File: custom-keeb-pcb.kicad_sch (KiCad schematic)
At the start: 34 parts, among them SW1 SW_Push, SW2 RotaryEncoder_Switch, U1 ATmega32U4-A, Y1 16MHz

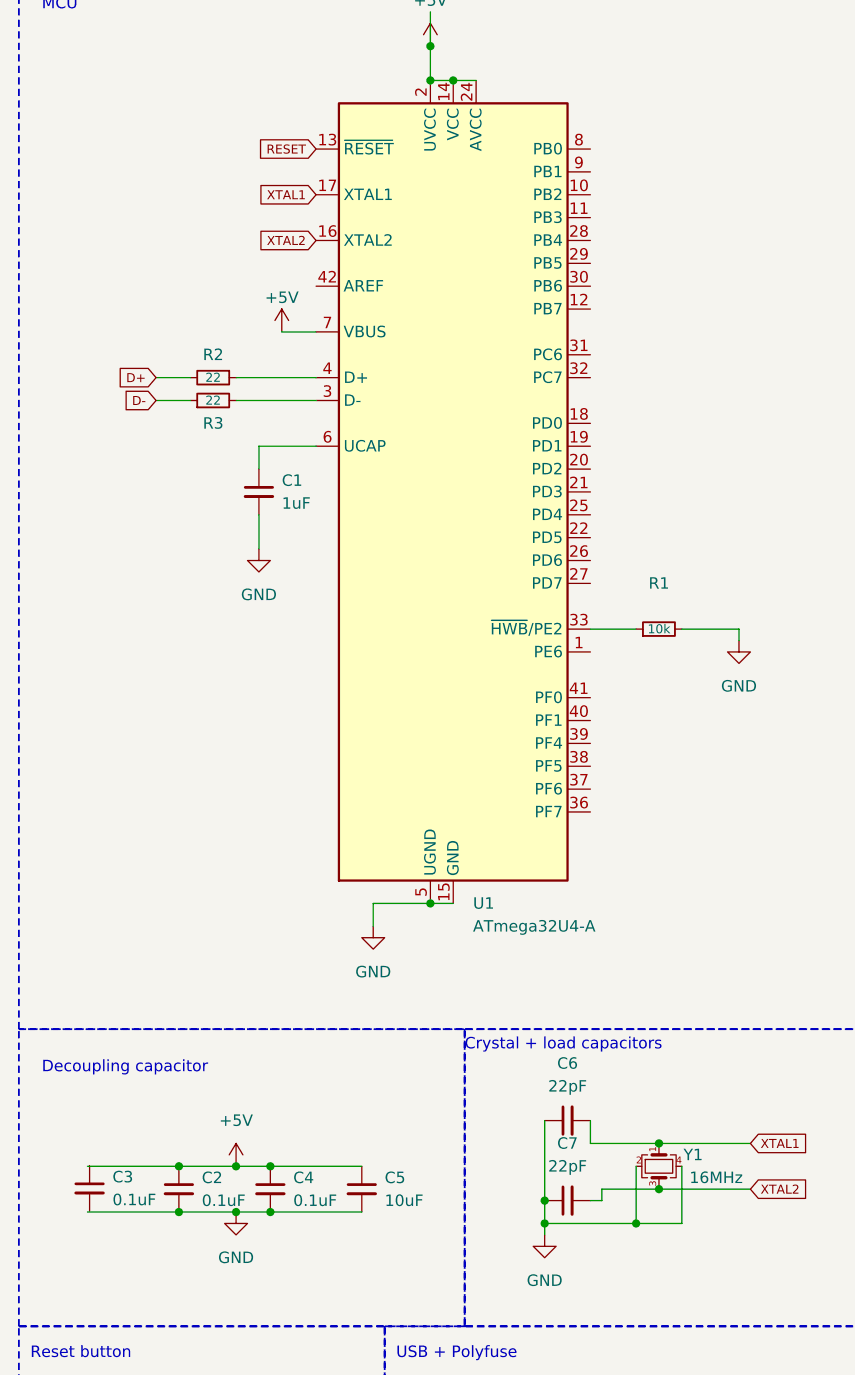
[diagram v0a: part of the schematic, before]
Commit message: Completed v1 of PCB design
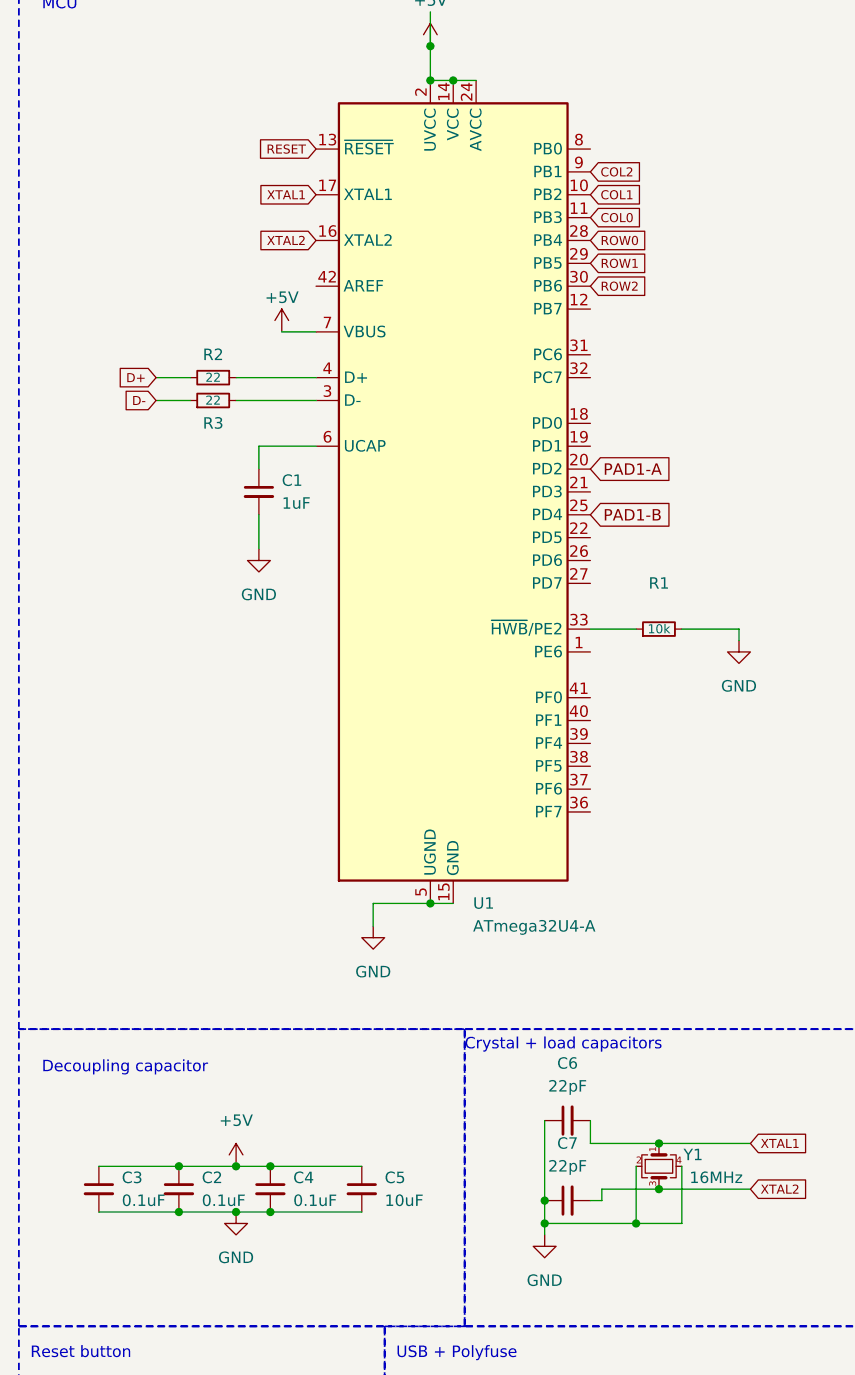
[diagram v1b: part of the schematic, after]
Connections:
- net +5V: now also C3.1
- net COL0: now also U1.11 (PB3)
- net COL1: now also U1.10 (PB2)
- net COL2: now also U1.9 (PB1)
- net GND: now also C3.2
- net PAD1-A: now also U1.20 (PD2)
- net PAD1-B: now also U1.25 (PD4)
- net ROW0: now also U1.28 (PB4)
- net ROW1: now also U1.29 (PB5)
- net ROW2: now also U1.30 (PB6)
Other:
- moved on the sheet: C3
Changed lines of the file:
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@@
   (junction (at 81.28 151.13) (diameter 0) (color 0 0 0 0)
   )
+  (junction (at 161.29 50.8) (diameter 0) (color 0 0 0 0)
+  )
+  (junction (at 30.48 149.86) (diameter 0) (color 0 0 0 0)
+  )
+  (junction (at 71.12 151.13) (diameter 0) (color 0 0 0 0)
+  )
+  (junction (at 153.67 76.2) (diameter 0) (color 0 0 0 0)
+  )
   (junction (at 30.48 144.78) (diameter 0) (color 0 0 0 0)
   )
-  (junction (at 161.29 50.8) (diameter 0) (color 0 0 0 0)
-  )
-  (junction (at 71.12 151.13) (diameter 0) (color 0 0 0 0)
-  )
-  (junction (at 153.67 76.2) (diameter 0) (color 0 0 0 0)
-  )
   (junction (at 186.69 66.04) (diameter 0) (color 0 0 0 0)
   )
@@
   (junction (at 173.99 66.04) (diameter 0) (color 0 0 0 0)
   )
-  (junction (at 30.48 149.86) (diameter 0) (color 0 0 0 0)
-  )
   (junction (at 83.82 147.32) (diameter 0) (color 0 0 0 0)
   )
@@
     (stroke (width 0) (type default))
   )
-  (wire (pts (xy 20.32 149.86) (xy 30.48 149.86))
-    (stroke (width 0) (type default))
-  )
   (wire (pts (xy 161.29 43.18) (xy 161.29 50.8))
     (stroke (width 0) (type default))
@@
     (stroke (width 0) (type default))
   )
-  (wire (pts (xy 20.32 144.78) (xy 30.48 144.78))
-    (stroke (width 0) (type default))
-  )
   (wire (pts (xy 166.37 71.12) (xy 168.91 71.12))
     (stroke (width 0) (type default))
@@
     (stroke (width 0) (type default))
   )
+  (wire (pts (xy 21.59 144.78) (xy 30.48 144.78))
+    (stroke (width 0) (type default))
+  )
   (wire (pts (xy 80.01 180.34) (xy 87.63 180.34))
     (stroke (width 0) (type default))
@@
   )
   (wire (pts (xy 77.47 147.32) (xy 83.82 147.32))
+    (stroke (width 0) (type default))
+  )
+  (wire (pts (xy 21.59 149.86) (xy 30.48 149.86))
     (stroke (width 0) (type default))
   )
@@
   (text "Decoupling capacitor" (at 15.24 134.62 0)
     (effects (font (size 1.27 1.27)) (justify left bottom))
+  )
+  (global_label "ROW1" (shape input) (at 76.2 44.45 0) (fields_autoplaced)
+    (effects (font (size 1 1)) (justify left))
+    (property "Intersheetrefs" "${INTERSHEET_REFS}" (at 82.6932 44.45 0)
+      (effects (font (size 1.27 1.27)) (justify left) hide)
+    )
+  )
+  (global_label "ROW0" (shape input) (at 76.2 41.91 0) (fields_autoplaced)
+    (effects (font (size 1 1)) (justify left))
+    (property "Intersheetrefs" "${INTERSHEET_REFS}" (at 82.6932 41.91 0)
+      (effects (font (size 1.27 1.27)) (justify left) hide)
+    )
+  )
+  (global_label "PAD1-B" (shape input) (at 76.2 72.39 0) (fields_autoplaced)
+    (effects (font (size 1.27 1.27)) (justify left))
+    (property "Intersheetrefs" "${INTERSHEET_REFS}" (at 86.8657 72.39 0)
+      (effects (font (size 1.27 1.27)) (justify left) hide)
+    )
   )
   (global_label "XTAL2" (shape input) (at 93.98 147.32 0) (fields_autoplaced)
@@
     )
   )
+  (global_label "ROW2" (shape input) (at 76.2 46.99 0) (fields_autoplaced)
+    (effects (font (size 1 1)) (justify left))
+    (property "Intersheetrefs" "${INTERSHEET_REFS}" (at 82.6932 46.99 0)
+      (effects (font (size 1.27 1.27)) (justify left) hide)
+    )
+  )
   (global_label "ROW1" (shape input) (at 142.24 76.2 180) (fields_autoplaced)
     (effects (font (size 1 1)) (justify right))
@@
     )
   )
+  (global_label "COL1" (shape input) (at 76.2 36.83 0) (fields_autoplaced)
+    (effects (font (size 1 1)) (justify left))
+    (property "Intersheetrefs" "${INTERSHEET_REFS}" (at 82.3598 36.83 0)
+      (effects (font (size 1.27 1.27)) (justify left) hide)
+    )
+  )
   (global_label "XTAL2" (shape input) (at 45.72 41.91 180) (fields_autoplaced)
     (effects (font (size 1 1)) (justify right))
@@
     )
   )
+  (global_label "PAD1-A" (shape input) (at 76.2 67.31 0) (fields_autoplaced)
+    (effects (font (size 1.27 1.27)) (justify left))
+    (property "Intersheetrefs" "${INTERSHEET_REFS}" (at 86.6843 67.31 0)
+      (effects (font (size 1.27 1.27)) (justify left) hide)
+    )
+  )
+  (global_label "COL2" (shape input) (at 76.2 34.29 0) (fields_autoplaced)
+    (effects (font (size 1 1)) (justify left))
+    (property "Intersheetrefs" "${INTERSHEET_REFS}" (at 82.3598 34.29 0)
+      (effects (font (size 1.27 1.27)) (justify left) hide)
+    )
+  )
+  (global_label "COL0" (shape input) (at 76.2 39.37 0) (fields_autoplaced)
+    (effects (font (size 1 1)) (justify left))
+    (property "Intersheetrefs" "${INTERSHEET_REFS}" (at 82.3598 39.37 0)
+      (effects (font (size 1.27 1.27)) (justify left) hide)
+    )
+  )
   (global_label "COL0" (shape input) (at 161.29 43.18 90) (fields_autoplaced)
     (effects (font (size 1 1)) (justify left))
@@
     )
   )
-  (symbol (lib_id "Device:C_Small") (at 20.5527 147.2357 0) (unit 1)
+  (symbol (lib_id "Device:C_Small") (at 21.59 147.32 0) (unit 1)
     (in_bom yes) (on_board yes) (dnp no) (fields_autoplaced)
-    (property "Reference" "C3" (at 23.0927 145.972 0)
+    (property "Reference" "C3" (at 24.13 146.0563 0)
       (effects (font (size 1.27 1.27)) (justify left))
     )
-    (property "Value" "0.1uF" (at 23.0927 148.512 0)
+    (property "Value" "0.1uF" (at 24.13 148.5963 0)
       (effects (font (size 1.27 1.27)) (justify left))
     )
-    (property "Footprint" "Capacitor_SMD:C_0805_2012Metric" (at 20.5527 147.2357 0)
-      (effects (font (size 1.27 1.27)) hide)
-    )
-    (property "Datasheet" "~" (at 20.5527 147.2357 0)
-      (effects (font (size 1.27 1.27)) hide)
-    )
+    (property "Footprint" "Capacitor_SMD:C_0805_2012Metric" (at 21.59 147.32 0)
+      (effects (font (size 1.27 1.27)) hide)
+    )
+    (property "Datasheet" "~" (at 21.59 147.32 0)
+      (effects (font (size 1.27 1.27)) hide)
+    )

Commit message: Finished v2 Design
Rerouted traces, added fill, added decals & text. Ready for printing
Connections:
- net COL0: now also U1.40 (PF1); no longer U1.11 (PB3)
- net COL1: now also U1.39 (PF4); no longer U1.10 (PB2)
- net COL2: now also U1.38 (PF5); no longer U1.9 (PB1)
- net ROW0: now also U1.9 (PB1); no longer U1.28 (PB4)
- net ROW1: now also U1.10 (PB2); no longer U1.29 (PB5)
- net ROW2: now also U1.11 (PB3); no longer U1.30 (PB6)
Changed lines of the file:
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@@
     (effects (font (size 1.27 1.27)) (justify left bottom))
   )
-  (global_label "ROW1" (shape input) (at 76.2 44.45 0) (fields_autoplaced)
+  (global_label "ROW1" (shape input) (at 76.2 36.83 0) (fields_autoplaced)
     (effects (font (size 1 1)) (justify left))
-    (property "Intersheetrefs" "${INTERSHEET_REFS}" (at 82.6932 44.45 0)
+    (property "Intersheetrefs" "${INTERSHEET_REFS}" (at 82.6932 36.83 0)
       (effects (font (size 1.27 1.27)) (justify left) hide)
     )
   )
-  (global_label "ROW0" (shape input) (at 76.2 41.91 0) (fields_autoplaced)
+  (global_label "ROW0" (shape input) (at 76.2 34.29 0) (fields_autoplaced)
     (effects (font (size 1 1)) (justify left))
-    (property "Intersheetrefs" "${INTERSHEET_REFS}" (at 82.6932 41.91 0)
+    (property "Intersheetrefs" "${INTERSHEET_REFS}" (at 82.6932 34.29 0)
       (effects (font (size 1.27 1.27)) (justify left) hide)
     )
@@
     )
   )
-  (global_label "ROW2" (shape input) (at 76.2 46.99 0) (fields_autoplaced)
+  (global_label "ROW2" (shape input) (at 76.2 39.37 0) (fields_autoplaced)
     (effects (font (size 1 1)) (justify left))
-    (property "Intersheetrefs" "${INTERSHEET_REFS}" (at 82.6932 46.99 0)
+    (property "Intersheetrefs" "${INTERSHEET_REFS}" (at 82.6932 39.37 0)
       (effects (font (size 1.27 1.27)) (justify left) hide)
     )
@@
     )
   )
-  (global_label "COL1" (shape input) (at 76.2 36.83 0) (fields_autoplaced)
+  (global_label "COL1" (shape input) (at 76.2 97.79 0) (fields_autoplaced)
     (effects (font (size 1 1)) (justify left))
-    (property "Intersheetrefs" "${INTERSHEET_REFS}" (at 82.3598 36.83 0)
+    (property "Intersheetrefs" "${INTERSHEET_REFS}" (at 82.3598 97.79 0)
       (effects (font (size 1.27 1.27)) (justify left) hide)
     )
@@
     )
   )
-  (global_label "COL2" (shape input) (at 76.2 34.29 0) (fields_autoplaced)
+  (global_label "COL2" (shape input) (at 76.2 100.33 0) (fields_autoplaced)
     (effects (font (size 1 1)) (justify left))
-    (property "Intersheetrefs" "${INTERSHEET_REFS}" (at 82.3598 34.29 0)
+    (property "Intersheetrefs" "${INTERSHEET_REFS}" (at 82.3598 100.33 0)
       (effects (font (size 1.27 1.27)) (justify left) hide)
     )
   )
-  (global_label "COL0" (shape input) (at 76.2 39.37 0) (fields_autoplaced)
+  (global_label "COL0" (shape input) (at 76.2 95.25 0) (fields_autoplaced)
     (effects (font (size 1 1)) (justify left))
-    (property "Intersheetrefs" "${INTERSHEET_REFS}" (at 82.3598 39.37 0)
+    (property "Intersheetrefs" "${INTERSHEET_REFS}" (at 82.3598 95.25 0)
       (effects (font (size 1.27 1.27)) (justify left) hide)
     )
